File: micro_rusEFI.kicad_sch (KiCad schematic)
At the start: 57 parts, among them J12 Conn_01x01, J13 Conn_01x01, J3 Conn_01x01, J4 Conn_02x05_Counter_Clockwise, J5 Conn_01x01, U3 molex_48pin_MRE, U7 XC6206 3.3V

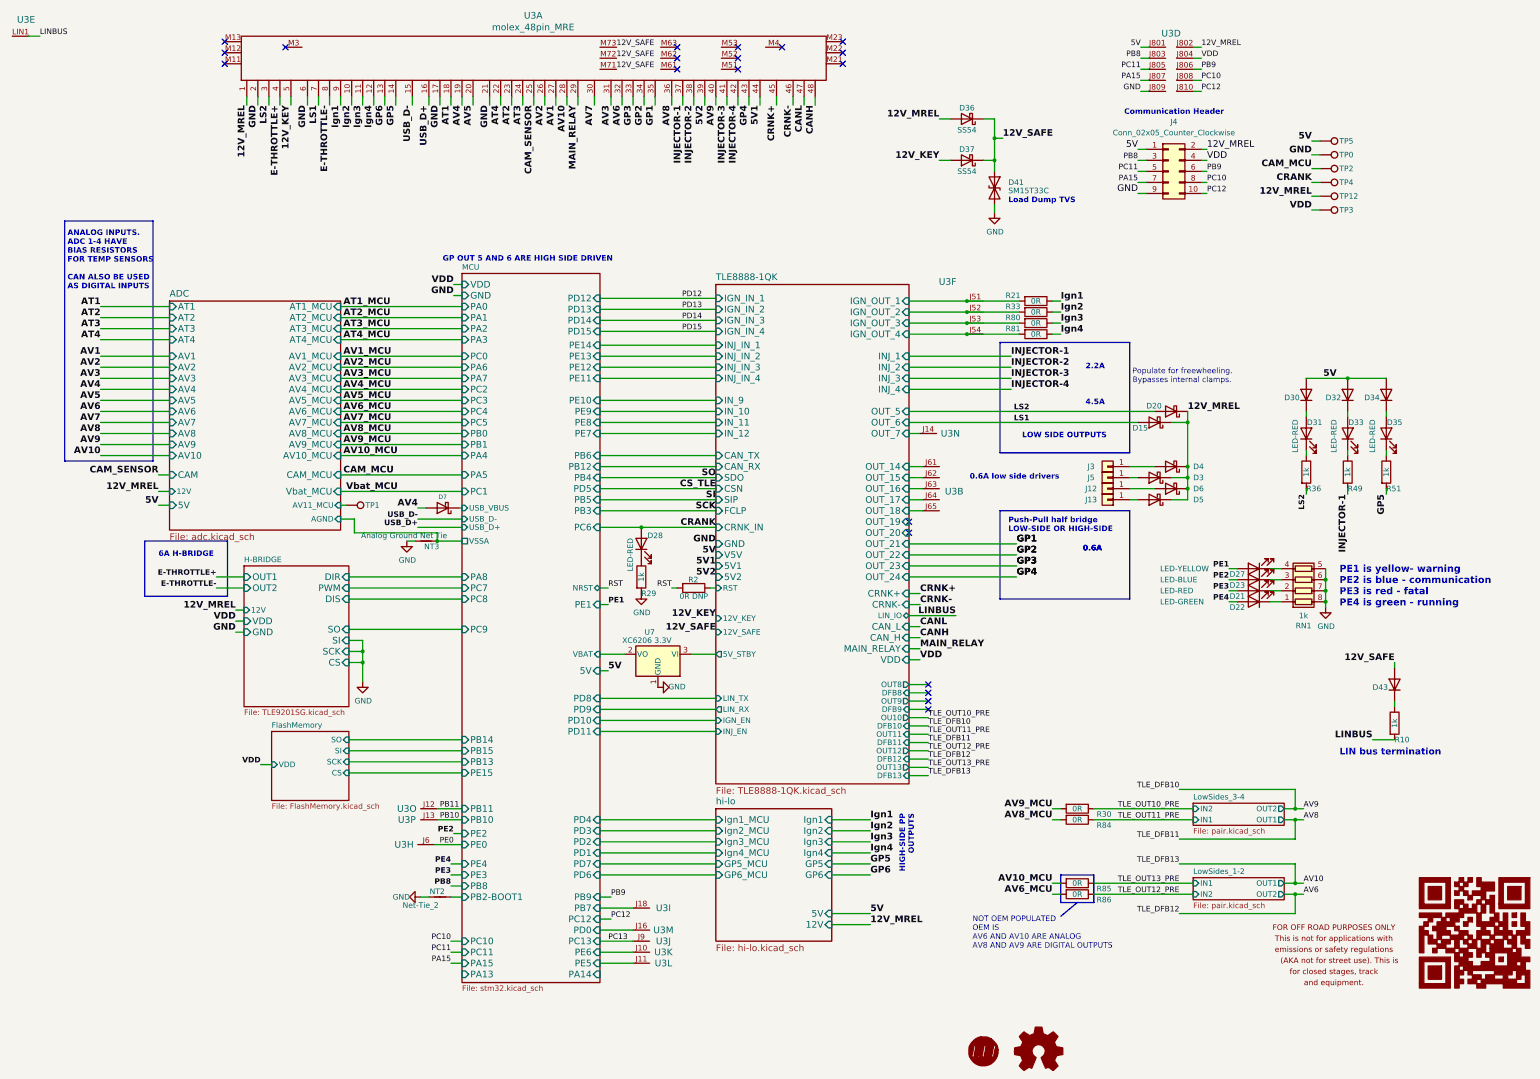
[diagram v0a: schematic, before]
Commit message: replaces micro b connector by usb-c
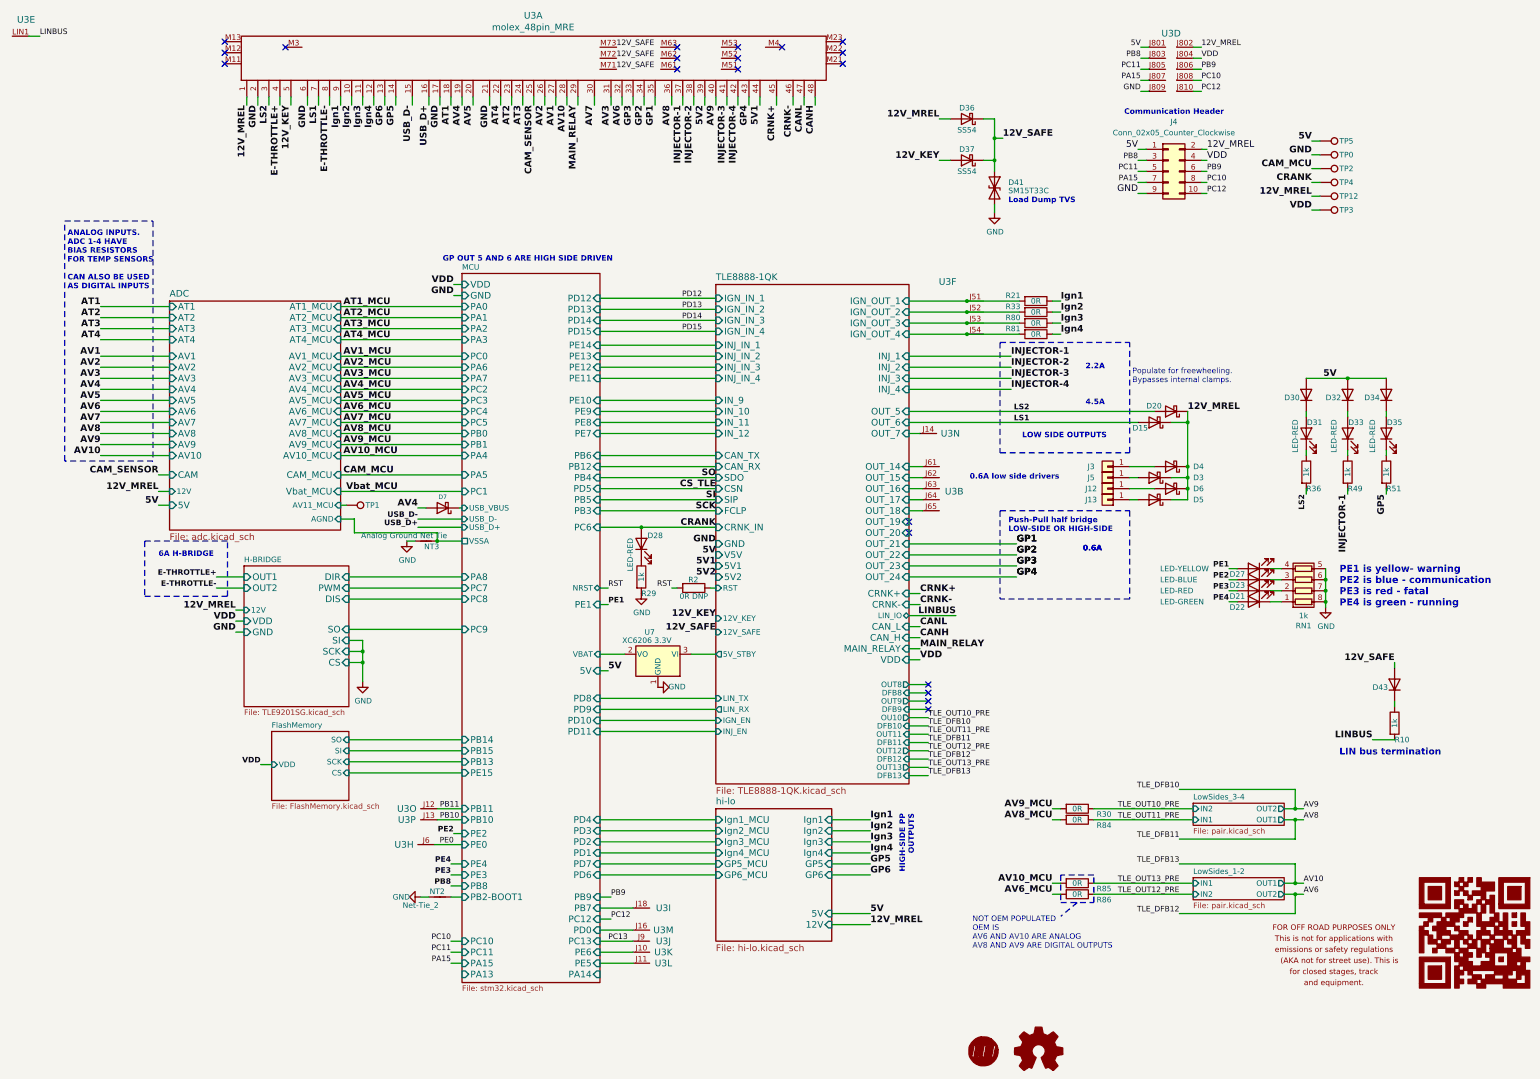
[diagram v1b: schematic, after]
